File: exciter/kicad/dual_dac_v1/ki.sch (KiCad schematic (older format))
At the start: 43 parts, among them U1 MCP4822, U2 TL052, U3 74HC594

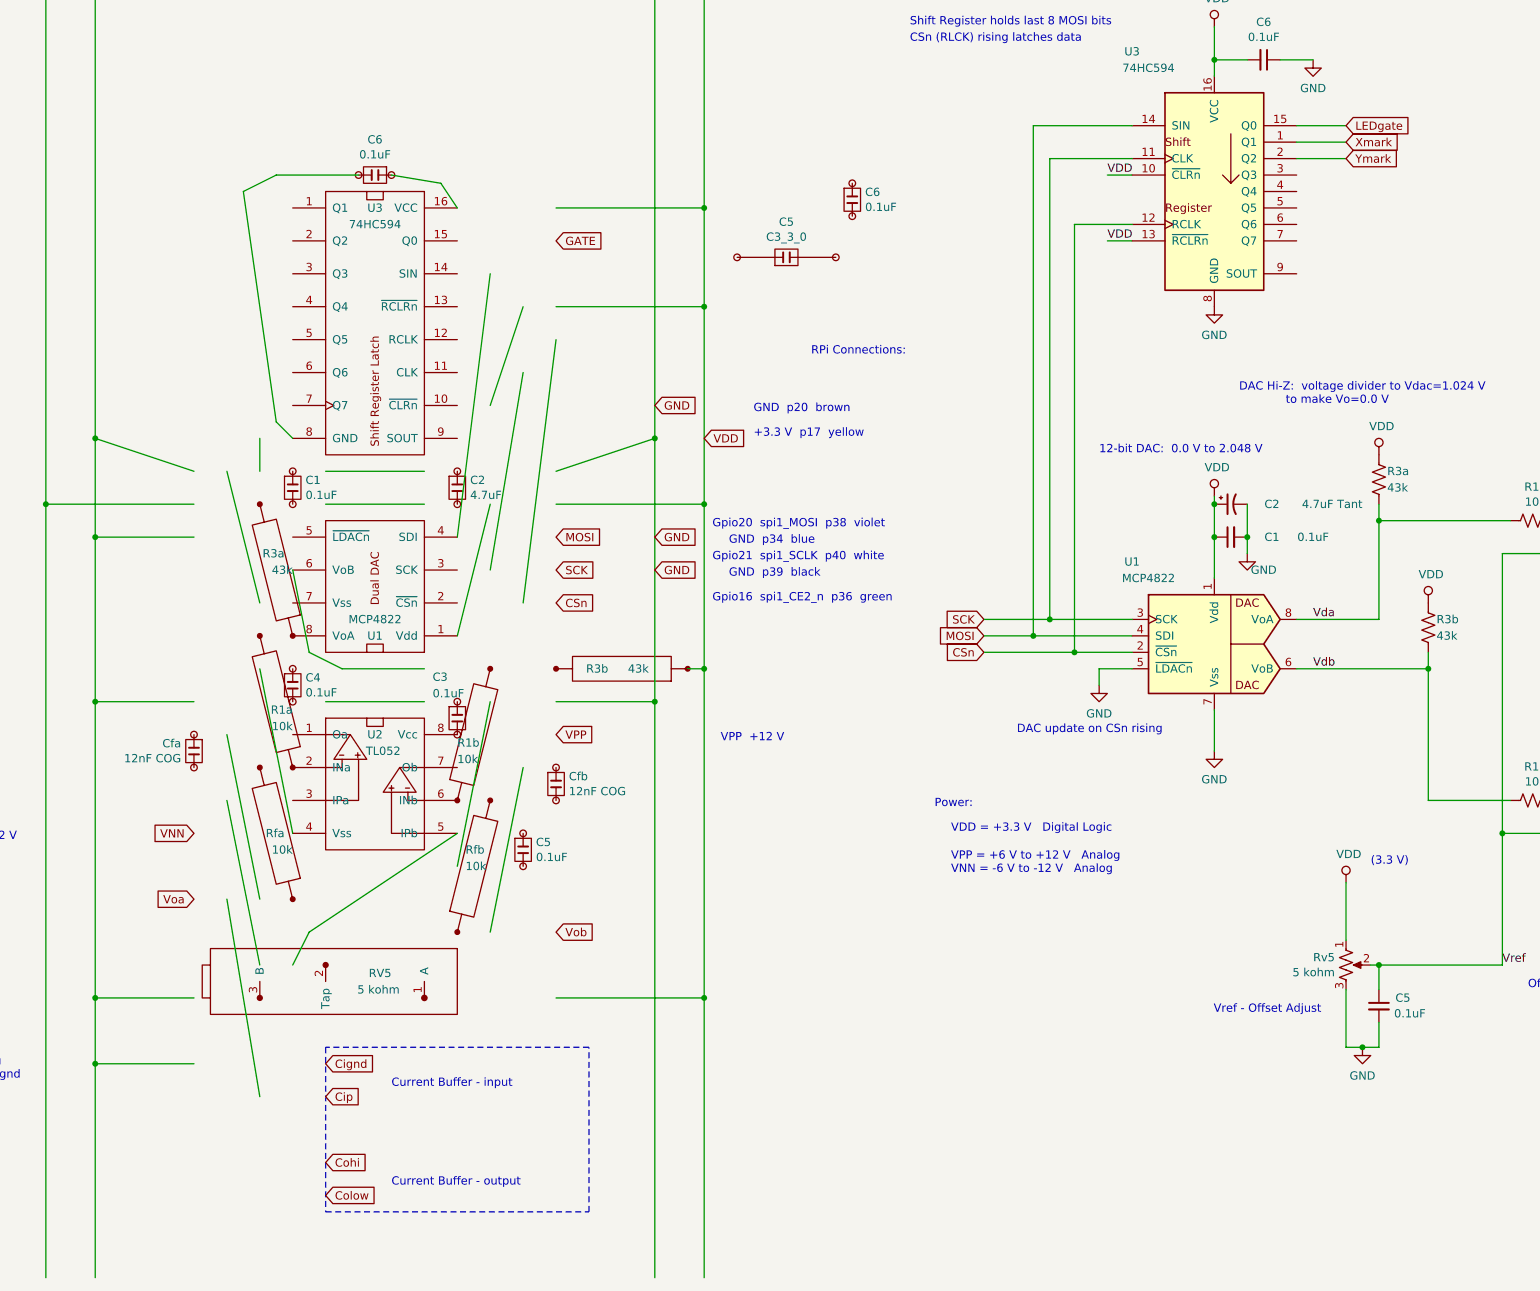
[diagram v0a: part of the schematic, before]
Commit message: Exciter:  rasta_mcp4822 and dual_dac_v1 fixes.
rasta_mcp4822:  Extended shift bits fix and configuration note.
dual_dac_v1:  v1.0.1 2023-07-05  Amark and Bmark labels on shift register.
    Fluxgate Current Driver identification.
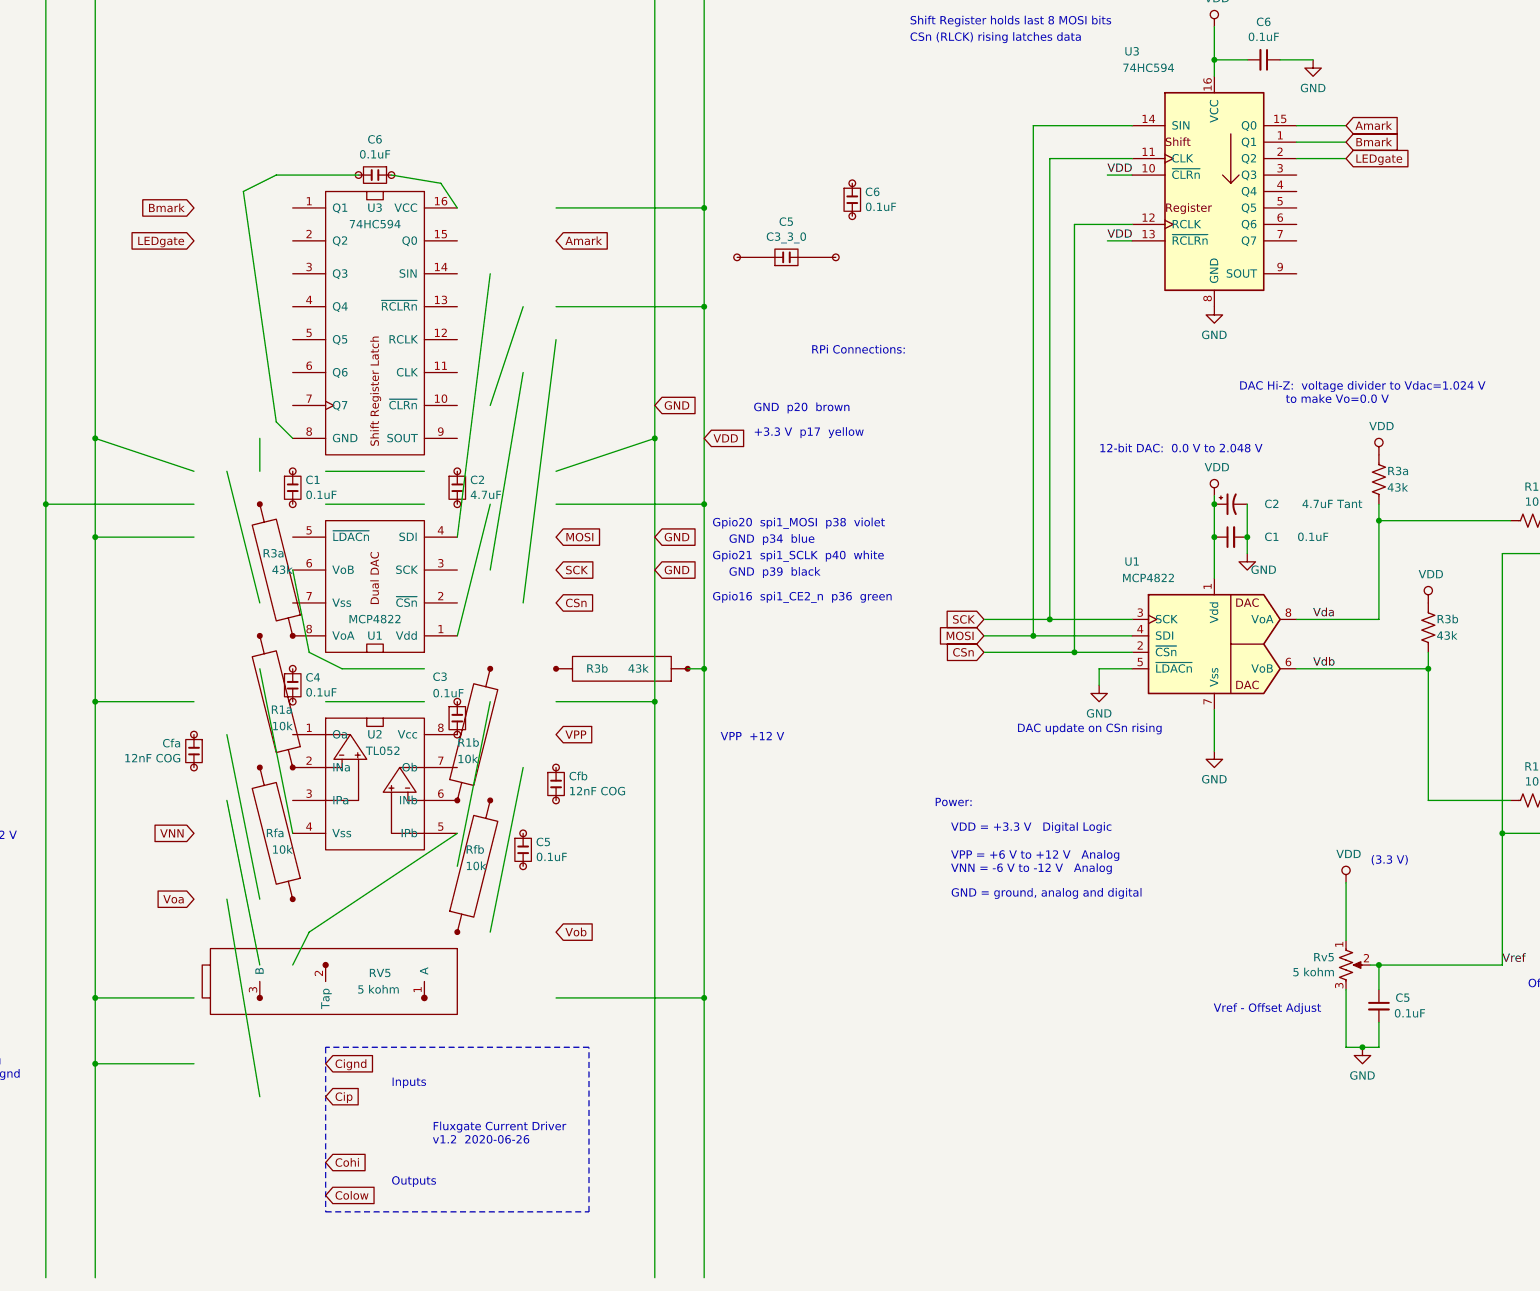
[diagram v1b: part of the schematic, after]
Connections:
- net labels added: Amark, Bmark
- net labels removed: GATE, Xmark, Ymark
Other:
- note added: "Fluxgate Current Driver\nv1.2 2020-06-26"
- note added: "GND = ground, analog and digital"
- note added: "Inputs"
- note added: "Outputs"
- note removed: "Current Buffer - input"
- note removed: "Current Buffer - output"
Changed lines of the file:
@@
 Sheet 1 1
 Title "dual_dac_v1/   2-Channel Voltage DAC"
-Date "2023-01-02"
-Rev "v1.0"
+Date "2023-07-05"
+Rev "v1.0.1"
 Comp "William A. Hudson"
-Comment1 ""
+Comment1 "v1.0.1  Sync mark corrections"
 Comment2 ""
 Comment3 ""
@@
 Text Notes 12300 9200 0    70   ~ 0
 Dual 12-bit DAC, 8 Digital out, 1.3 kHz LP Filter, Full Scale +-1.024 V
-Text GLabel 4800 4000 2    50   Input ~ 0
-GATE
 Text Notes 6000 5050 0    50   ~ 0
 GND  p20  brown
@@
 DAC update on CSn rising
 Text Notes 3800 9150 0    50   ~ 0
-Current Buffer - input
+Inputs
 Text Notes 3800 9750 0    50   ~ 0
-Current Buffer - output
+Outputs
 Wire Notes Line
 	3400 8900 3400 9900
@@
 Wire Wire Line
 	9200 2900 9400 2900
+Text GLabel 9600 3500 2    50   Input ~ 0
+LEDgate
 Text GLabel 9600 3300 2    50   Input ~ 0
-LEDgate
+Amark
 Text GLabel 9600 3400 2    50   Input ~ 0
-Xmark
-Text GLabel 9600 3500 2    50   Input ~ 0
-Ymark
+Bmark
 Wire Wire Line
 	11500 6900 11900 6900
@@
 Text Notes 12300 8900 0    50   ~ 0
 Inverting output:  Vo = (0.0005 V) * (2048 - Code)\n    Code = {0..4095}
+Text GLabel 2600 3800 0    50   Input ~ 0
+Bmark
+Text GLabel 4800 4000 2    50   Input ~ 0
+Amark
+Text GLabel 2600 4000 0    50   Input ~ 0
+LEDgate
+Text Notes 4050 9500 0    50   ~ 0
+Fluxgate Current Driver\nv1.2  2020-06-26
+Text Notes 7200 8000 0    50   ~ 0
+GND = ground, analog and digital
 $EndSCHEMATC
